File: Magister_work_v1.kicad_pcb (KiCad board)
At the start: 4 copper layers, 50.5 x 81 mm, 151 parts, among them J1 Conn_01x02_Pin, J10 Conn_01x06_Pin, J11 Conn_01x03_Pin, J12 Conn_01x03_Pin, J13 Conn_01x03_Pin, J14 Conn_01x03_Pin, J15 Conn_01x02_Pin, J17 Conn_01x04_Pin, J2 Conn_01x03_Pin, J3 Conn_01x03_Pin, J4 Conn_01x03_Pin, J5 Conn_01x03_Pin, J6 Conn_01x04_Pin, J7 Conn_01x02_Pin, J8 Conn_01x06_Pin, J9 Conn_01x02_Pin, Q1 AO3400A, Q2 AO3400A, U10 LSM6DS3, U11 MPU-6500, U12 BMI270, U2 XC6206P332MR, U3 Ai-Thinker-Ra-01, U4 MCP6001-OT, U5 AMS1117-3.3, U6 XL1509-5.0, U7 STM32F407VETx, U8 AT24C256, U9 Ai-Thinker-Ra-01SH, Y1 X322525MQB4SI, Y2 SMD03215C2

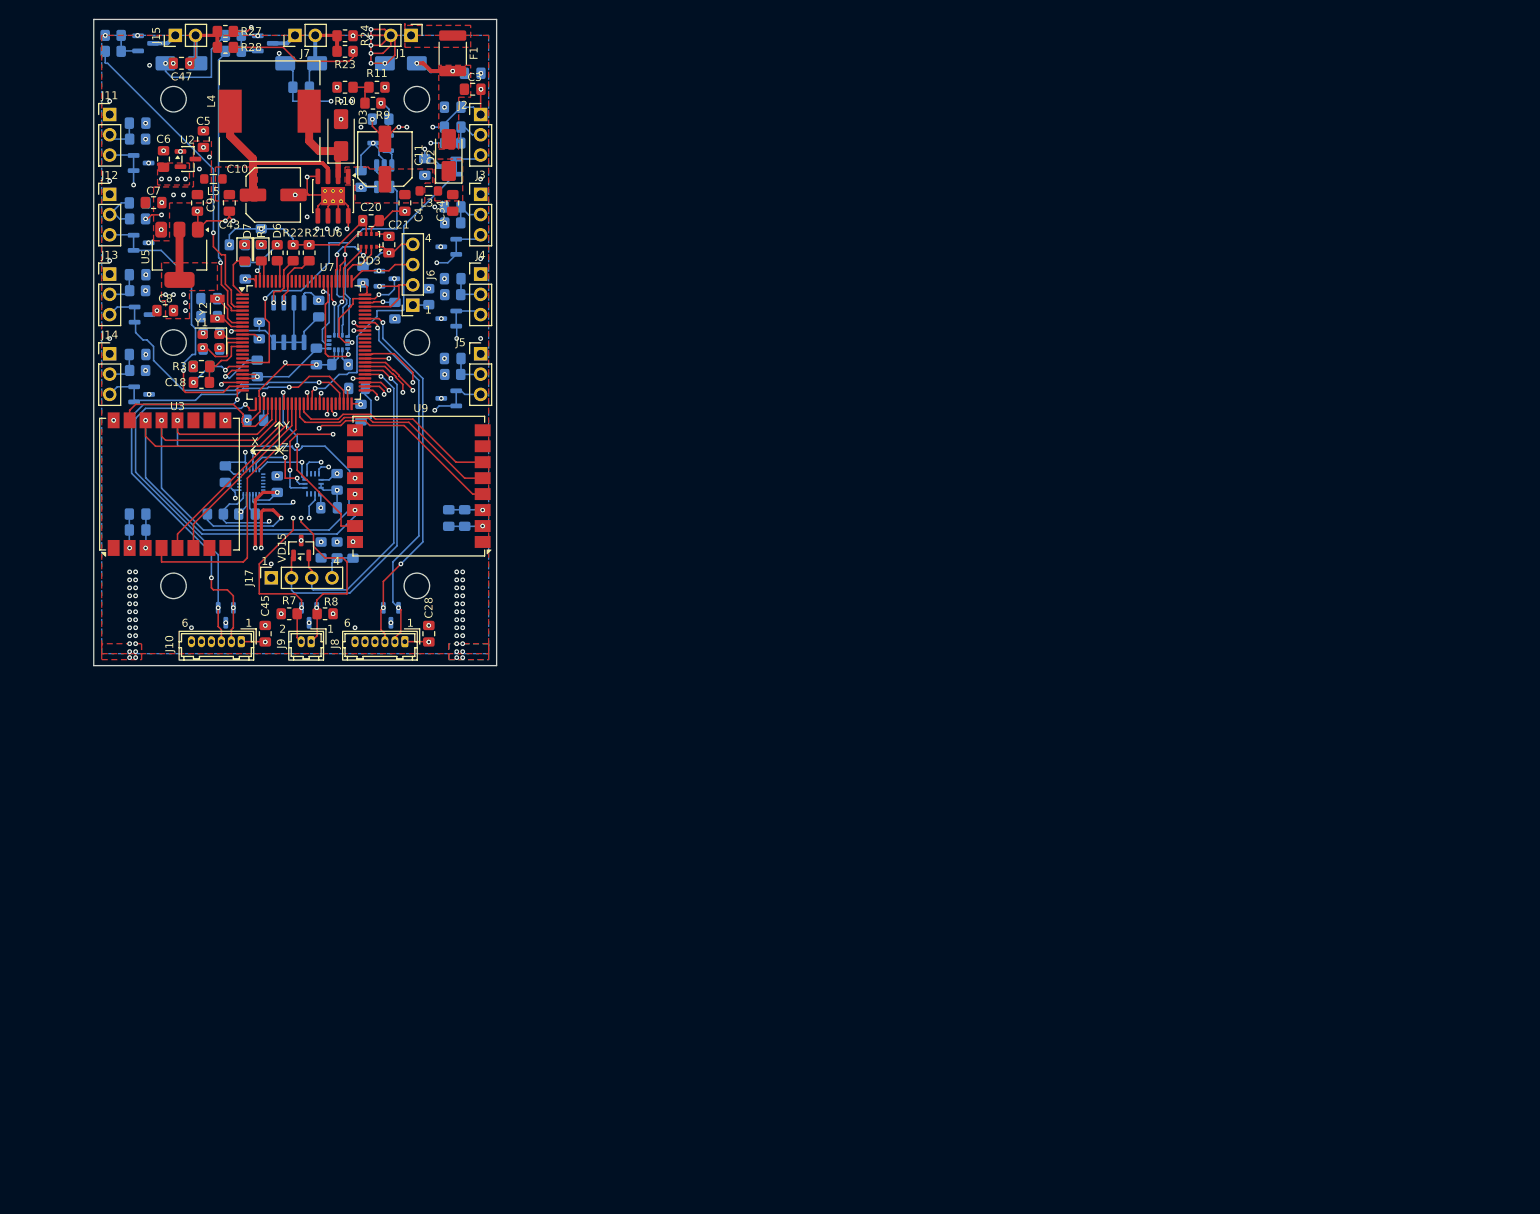
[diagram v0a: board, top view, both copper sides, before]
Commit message: feat:убрал часть с батарейным питанием, убрал лишние элементы со старого проекта
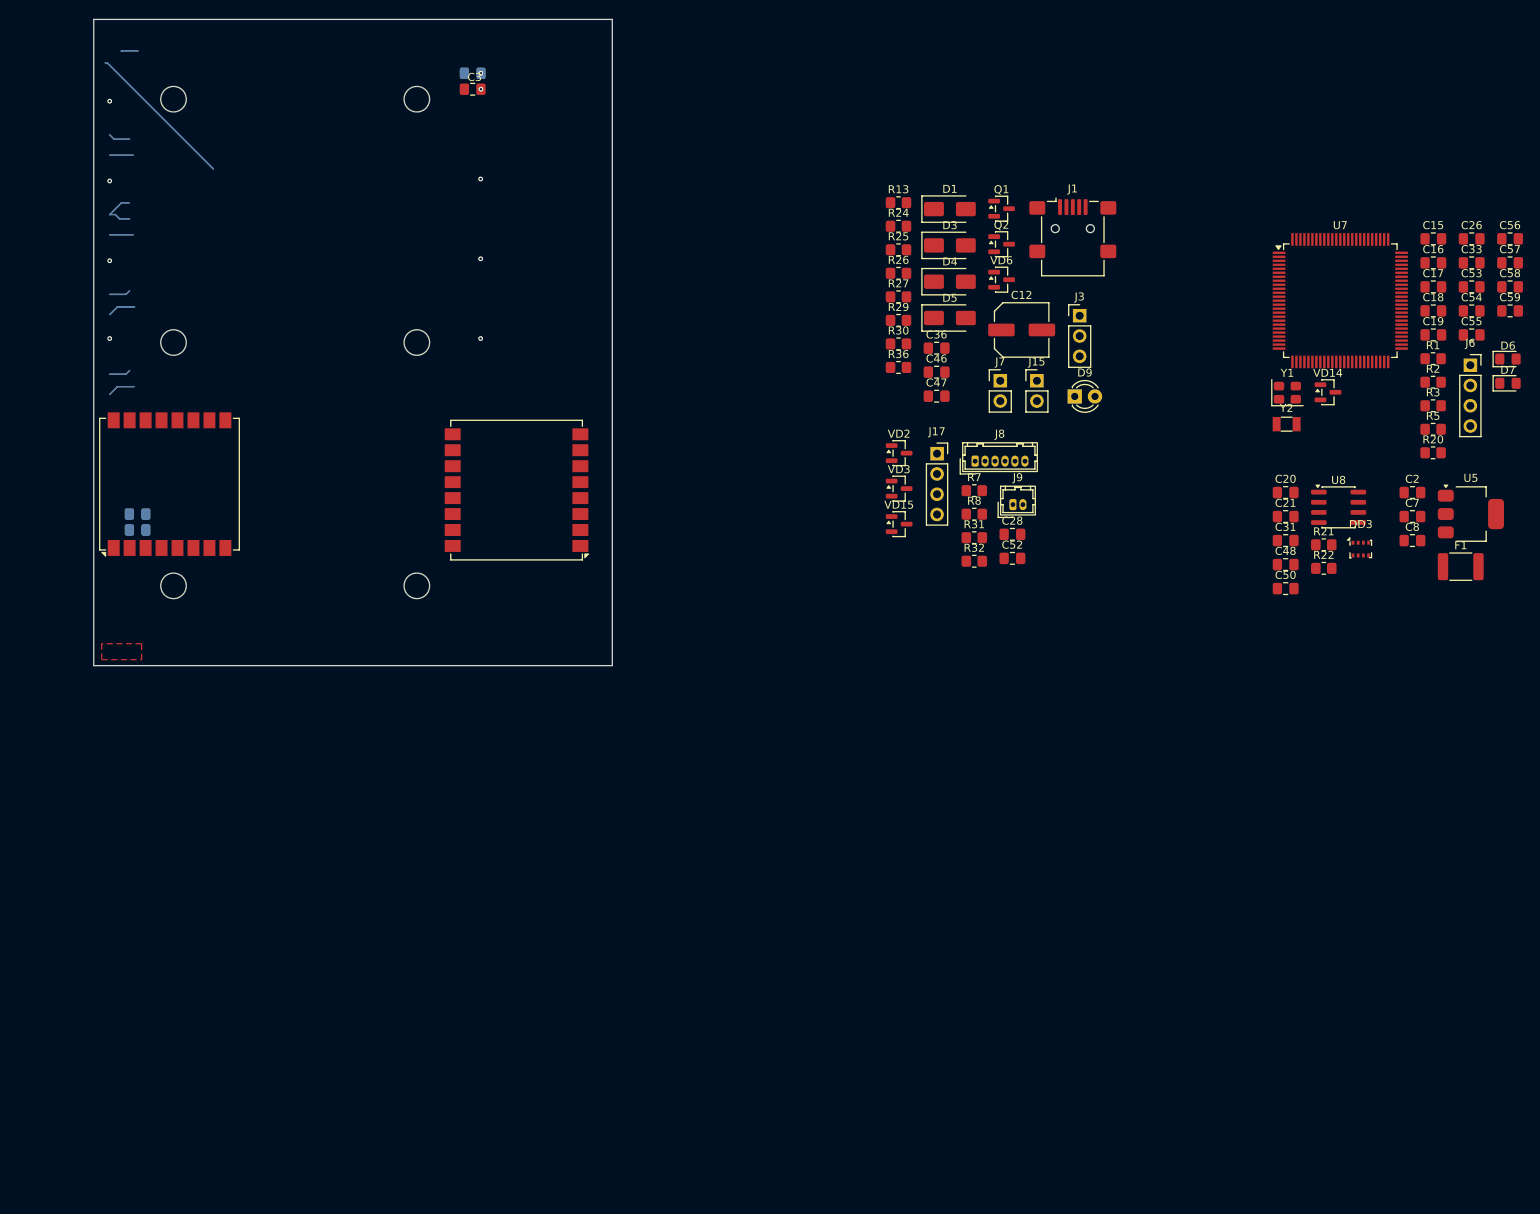
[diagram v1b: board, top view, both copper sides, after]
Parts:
- removed C10, C11: 100u, Capacitor_SMD:C_Elec_6.3x7.7
- removed C14, C22, C23, C24, C25, C27, C29, C30, C34, C35, C37, C38, C39, C4, C40, C41, C42, C43, C44, C45, C5, C51, C6, C9: 0.1u, Capacitor_SMD:C_0805_2012Metric_Pad1.18x1.45mm_HandSolder
- removed D2: SS36, Diode_SMD:D_SMA
- removed J10: Conn_01x06_Pin, Connector_Hirose:Hirose_DF13-06P-1.25DSA_1x06_P1.25mm_Vertical
- removed J11, J12, J13, J14, J2, J4, J5: Conn_01x03_Pin, Connector_PinHeader_2.54mm:PinHeader_1x03_P2.54mm_Vertical
- removed L3, L5: BLM21PG121SN1D, Inductor_SMD:L_0805_2012Metric_Pad1.05x1.20mm_HandSolder
- removed L4: 47uH, Inductor_SMD:L_12x12mm_H8mm
- removed R10: 1k, Resistor_SMD:R_0805_2012Metric_Pad1.20x1.40mm_HandSolder
- removed R11, R4: 10k, Resistor_SMD:R_0805_2012Metric_Pad1.20x1.40mm_HandSolder
- removed R12, R14, R15, R16, R17, R18, R19, R23, R28: 0, Resistor_SMD:R_0805_2012Metric_Pad1.20x1.40mm_HandSolder
- removed R9: 3k, Resistor_SMD:R_0805_2012Metric_Pad1.20x1.40mm_HandSolder
- removed U10: LSM6DS3, Package_LGA:LGA-14_3x2.5mm_P0.5mm_LayoutBorder3x4y
- removed U11: MPU-6500, Sensor_Motion:InvenSense_QFN-24_3x3mm_P0.4mm
- removed U12: BMI270, Package_LGA:Bosch_LGA-14_3x2.5mm_P0.5mm
- removed U2: XC6206P332MR, Package_TO_SOT_SMD:SOT-23
- removed U4: MCP6001-OT, Package_TO_SOT_SMD:SOT-23-5_HandSoldering
- removed U6: XL1509-5.0, Package_SO:SOIC-8-1EP_3.9x4.9mm_P1.27mm_EP2.29x3mm_ThermalVias
- removed VD10, VD11, VD12, VD13, VD4, VD5, VD7, VD8, VD9: GSOT03C-E3-08, Package_TO_SOT_SMD:SOT-23
- added C12: 100u, Capacitor_SMD:C_Elec_6.3x7.7, F.Cu at (146.3, 68.9)
- added D9: LED, LED_THT:LED_D3.0mm_Clear, F.Cu at (153.0, 77.3)
- added R36: 330, Resistor_SMD:R_0805_2012Metric_Pad1.20x1.40mm_HandSolder, F.Cu at (130.9, 73.6)
- C1: value 0.01u -> 0.1u
- C15, C16, C17, C19, C2, C26, C31, C33, C36, C46, C48, C50, C52, C53, C54, C55, C56, C57, C58, C59, D4, D5, Q1, Q2, R13, R2, R20, R25, R26, R29, R30, R31, R32, R5, U8, VD14, VD2, VD3, VD6: moved to F.Cu
- C3: value 1u -> 0.1u
- D1: value SMAJ30CA -> SS32; moved to F.Cu
- D3: value SS36 -> SMAJ5.0CA
- J1: value Conn_01x02_Pin -> USB_B_Mini; footprint Connector_PinHeader_2.54mm:PinHeader_1x02_P2.54mm_Vertical -> Connector_USB:USB_Mini-B_Lumberg_2486_01_Horizontal
- moved U5 165.1 mm to (202.6, 92.0), turned to 0 degrees
- moved C56 163.4 mm to (207.5, 57.5)
- moved C58 163.1 mm to (207.5, 63.5)
- moved C59 163.1 mm to (207.5, 66.5), turned to 0 degrees
- moved C7 162.6 mm to (195.3, 92.3), turned to 0 degrees
- moved C26 160.0 mm to (202.7, 57.5), turned to 0 degrees
- moved D7 159.2 mm to (207.3, 75.6), turned to 0 degrees
- moved C8 159.0 mm to (195.3, 95.3), turned to 0 degrees
- moved C55 158.0 mm to (202.7, 69.5)
- moved D6 156.8 mm to (207.3, 72.6), turned to 0 degrees
- moved C18 154.6 mm to (197.9, 66.5), turned to 0 degrees
- moved R3 154.4 mm to (197.9, 78.4)
- moved C53 153.7 mm to (202.7, 63.5), turned to 0 degrees
- moved C54 152.4 mm to (202.7, 66.5), turned to 0 degrees
- moved C33 152.2 mm to (202.7, 60.5), turned to 0 degrees
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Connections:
- net +12V_1 renamed Net-(F1-A1)
- C1 pad 1: +12V_in -> +5V_in
- C2 pad 1: +12V_in -> +5V_in
- C3 pad 1: +12V_in -> +5V_in
- C8 pad 1: +3V3D -> +3V3
- D1 pad 1: GND -> +5V
- D1 pad 2: +12V_in -> +5V_in
- D3 pad 1: Net-(D3-K) -> GND
- D3 pad 2: GND -> +5V_in
- F1 pad 2: +12V_in -> +5V_in
- J1 pad 2: GND -> unconnected-(J1-D--Pad2)
- U5 pad 2: +3V3D -> +3V3
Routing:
- net GND: track 243.9 -> 0.00 mm, vias 144 -> 9
- net +3V3A: track 154.5 -> 0.00 mm, vias 9 -> 0
- net +5V: track 153.2 -> 0.00 mm, vias 21 -> 0
- net +3V3D: track 124.3 -> 0.00 mm, vias 31 -> 0
- net MOSI_LoRa: track 61.2 -> 0.00 mm, vias 2 -> 0
- net MISO_LoRa: track 57.4 -> 0.00 mm, vias 2 -> 0
- net MPU_INT: track 54.9 -> 0.00 mm, vias 2 -> 0
- net BN_880_SCL: track 54.4 -> 0.00 mm, vias 3 -> 0
- net BN_880_SDA: track 53.3 -> 0.00 mm, vias 3 -> 0
- net DEBUG_TX1: track 50.6 -> 0.00 mm, vias 3 -> 0
- net MPU_CS: track 50.0 -> 0.00 mm, vias 2 -> 0
- net DEBUG_RX1: track 49.5 -> 0.00 mm, vias 2 -> 0
- net BN_880_RX: track 46.9 -> 0.00 mm, vias 3 -> 0
- net BN_880_TX: track 45.6 -> 0.00 mm, vias 2 -> 0
- net PWM1: track 45.3 -> 0.00 mm, vias 1 -> 0
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- removed copper zone on F.Cu, net +12V
- removed copper zone on F.Cu, net +12V_in
- removed copper zone on F.Cu, net +3V3A
- removed copper zone on In2.Cu, net +3V3A
- removed copper zone on F.Cu, net +3V3D
- removed copper zone on In1.Cu, net +3V3D
- removed copper zone on In2.Cu, net +3V3D
- removed copper zone on F.Cu, net +5V
- removed copper zone on In2.Cu, net +5V
- removed copper zone on B.Cu, net GND
- removed copper zone on In2.Cu, net GND
- removed copper zone on F.Cu, net Net-(D2-K)
- removed copper zone on F.Cu, net Net-(F1-A1)
- removed copper zone on F.Cu, net Net-(U6-FB)
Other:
- board size 50.5 x 81 mm -> 65 x 81 mm
- board text removed: "1"
- board text removed: "2"
- board text removed: "4"
- board text removed: "6"
- board text removed: "X"
- board text removed: "Y"
- board text removed: "Z"

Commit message: feaat: добавлены светодиоды, кнопки и недостающие элементы защиты питания
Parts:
- removed R25, R29: 100, Resistor_SMD:R_0805_2012Metric_Pad1.20x1.40mm_HandSolder
- added C4: 0.1u, Capacitor_SMD:C_0805_2012Metric_Pad1.18x1.45mm_HandSolder, F.Cu at (182.7, 155.8)
- added C60: 0.1u, Capacitor_SMD:C_0805_2012Metric_Pad1.18x1.45mm_HandSolder, F.Cu at (130.1, 132.9)
- added C61: 0.1u, Capacitor_SMD:C_0805_2012Metric_Pad1.18x1.45mm_HandSolder, F.Cu at (130.1, 135.9)
- added C62: 0.1u, Capacitor_SMD:C_0805_2012Metric_Pad1.18x1.45mm_HandSolder, F.Cu at (130.1, 138.9)
- added C63: 0.1u, Capacitor_SMD:C_0805_2012Metric_Pad1.18x1.45mm_HandSolder, F.Cu at (130.1, 141.9)
- added C64: 0.1u, Capacitor_SMD:C_0805_2012Metric_Pad1.18x1.45mm_HandSolder, F.Cu at (134.9, 132.9)
- added C65: 0.1u, Capacitor_SMD:C_0805_2012Metric_Pad1.18x1.45mm_HandSolder, F.Cu at (134.9, 135.9)
- added C66: 0.1u, Capacitor_SMD:C_0805_2012Metric_Pad1.18x1.45mm_HandSolder, F.Cu at (134.9, 138.9)
- added C67: 0.1u, Capacitor_SMD:C_0805_2012Metric_Pad1.18x1.45mm_HandSolder, F.Cu at (134.9, 141.9)
- added C68: 0.1u, Capacitor_SMD:C_0805_2012Metric_Pad1.18x1.45mm_HandSolder, F.Cu at (139.7, 132.9)
- added C69: 0.1u, Capacitor_SMD:C_0805_2012Metric_Pad1.18x1.45mm_HandSolder, F.Cu at (139.7, 135.9)
- added C70: 0.1u, Capacitor_SMD:C_0805_2012Metric_Pad1.18x1.45mm_HandSolder, F.Cu at (139.7, 138.9)
- added C71: 0.1u, Capacitor_SMD:C_0805_2012Metric_Pad1.18x1.45mm_HandSolder, F.Cu at (139.7, 141.9)
- added D10: LED, LED_THT:LED_D3.0mm, F.Cu at (173.6, 114.0)
- added D11: LED, LED_THT:LED_D3.0mm, F.Cu at (173.6, 119.4)
- added D12: LED, LED_THT:LED_D3.0mm, F.Cu at (173.6, 124.9)
- added D13: LED, LED_THT:LED_D3.0mm, F.Cu at (173.6, 130.4)
- added D14: LED, LED_THT:LED_D3.0mm, F.Cu at (173.6, 135.8)
- added D15: SMBJ5.0CA, Diode_SMD:D_SMB, F.Cu at (176.1, 152.4)
- added D8: LED, LED_THT:LED_D3.0mm, F.Cu at (173.6, 108.5)
- added Q3: PDTC143ET, Package_TO_SOT_SMD:SOT-23-3, F.Cu at (180.4, 108.0)
- added Q4: PDTC143ET, Package_TO_SOT_SMD:SOT-23-3, F.Cu at (180.4, 112.4)
- added Q5: PDTC143ET, Package_TO_SOT_SMD:SOT-23-3, F.Cu at (180.4, 116.9)
- added Q6: PDTC143ET, Package_TO_SOT_SMD:SOT-23-3, F.Cu at (180.4, 121.3)
- added Q7: PDTC143ET, Package_TO_SOT_SMD:SOT-23-3, F.Cu at (180.4, 125.8)
- added Q8: PDTC143ET, Package_TO_SOT_SMD:SOT-23-3, F.Cu at (180.4, 130.2)
- added R11: 220, Resistor_SMD:R_0805_2012Metric_Pad1.20x1.40mm_HandSolder, F.Cu at (185.3, 113.1)
- added R12: 220, Resistor_SMD:R_0805_2012Metric_Pad1.20x1.40mm_HandSolder, F.Cu at (185.3, 116.1)
- added R14: 220, Resistor_SMD:R_0805_2012Metric_Pad1.20x1.40mm_HandSolder, F.Cu at (185.3, 119.0)
- added R15: 10k, Resistor_SMD:R_0805_2012Metric_Pad1.20x1.40mm_HandSolder, F.Cu at (182.4, 142.0)
- added R16: 220, Resistor_SMD:R_0805_2012Metric_Pad1.20x1.40mm_HandSolder, F.Cu at (185.3, 122.0)
- added R28: 100, Resistor_SMD:R_0805_2012Metric_Pad1.20x1.40mm_HandSolder, F.Cu at (144.5, 132.9)
- added R33: 100, Resistor_SMD:R_0805_2012Metric_Pad1.20x1.40mm_HandSolder, F.Cu at (144.5, 135.8)
- added R34: 100, Resistor_SMD:R_0805_2012Metric_Pad1.20x1.40mm_HandSolder, F.Cu at (144.5, 138.8)
- added R35: 100, Resistor_SMD:R_0805_2012Metric_Pad1.20x1.40mm_HandSolder, F.Cu at (144.5, 141.7)
- added R37: 100, Resistor_SMD:R_0805_2012Metric_Pad1.20x1.40mm_HandSolder, F.Cu at (149.3, 132.9)
- added R38: 100, Resistor_SMD:R_0805_2012Metric_Pad1.20x1.40mm_HandSolder, F.Cu at (149.3, 135.8)
- added R39: 100, Resistor_SMD:R_0805_2012Metric_Pad1.20x1.40mm_HandSolder, F.Cu at (149.3, 138.8)
- added R40: 100, Resistor_SMD:R_0805_2012Metric_Pad1.20x1.40mm_HandSolder, F.Cu at (149.3, 141.7)
- added R41: 100, Resistor_SMD:R_0805_2012Metric_Pad1.20x1.40mm_HandSolder, F.Cu at (154.0, 132.9)
- added R42: 100, Resistor_SMD:R_0805_2012Metric_Pad1.20x1.40mm_HandSolder, F.Cu at (154.0, 135.8)
- added R43: 100, Resistor_SMD:R_0805_2012Metric_Pad1.20x1.40mm_HandSolder, F.Cu at (154.0, 138.8)
- added R44: 100, Resistor_SMD:R_0805_2012Metric_Pad1.20x1.40mm_HandSolder, F.Cu at (154.0, 141.7)
- added R45: 220, Resistor_SMD:R_0805_2012Metric_Pad1.20x1.40mm_HandSolder, F.Cu at (182.4, 145.0)
- added R46: 220, Resistor_SMD:R_0805_2012Metric_Pad1.20x1.40mm_HandSolder, F.Cu at (182.4, 147.9)
- added R6: 220, Resistor_SMD:R_0805_2012Metric_Pad1.20x1.40mm_HandSolder, F.Cu at (185.3, 107.2)
- added R9: 220, Resistor_SMD:R_0805_2012Metric_Pad1.20x1.40mm_HandSolder, F.Cu at (185.3, 110.2)
- added SW1: SW_Push, Button_Switch_THT:SW_PUSH_6mm, F.Cu at (46.2, 50.8)
- added SW10: SW_Push, Button_Switch_THT:SW_PUSH_6mm, F.Cu at (161.4, 107.8)
- added SW11: SW_Push, Button_Switch_THT:SW_PUSH_6mm, F.Cu at (161.4, 116.3)
- added SW12: SW_Push, Button_Switch_THT:SW_PUSH_6mm, F.Cu at (161.4, 124.9)
- added SW2: SW_Push, Button_Switch_THT:SW_PUSH_6mm, F.Cu at (62.2, 50.8)
- added SW3: SW_Push, Button_Switch_THT:SW_PUSH_6mm, F.Cu at (129.7, 124.9)
- added SW4: SW_Push, Button_Switch_THT:SW_PUSH_6mm, F.Cu at (54.2, 43.2)
- added SW5: SW_Push, Button_Switch_THT:SW_PUSH_6mm, F.Cu at (54.2, 58.2)
- added SW6: SW_Push, Button_Switch_THT:SW_PUSH_6mm, F.Cu at (140.3, 124.9)
- added SW7: SW_Push, Button_Switch_THT:SW_PUSH_6mm, F.Cu at (150.8, 107.8)
- added SW8: SW_Push, Button_Switch_THT:SW_PUSH_6mm, F.Cu at (150.8, 116.3)
- added SW9: SW_Push, Button_Switch_THT:SW_PUSH_6mm, F.Cu at (150.8, 124.9)
- added U10: SRV05-4, Package_TO_SOT_SMD:SOT-23-6, F.Cu at (182.9, 152.1)
- added VD10: GSOT03C-E3-08, Package_TO_SOT_SMD:SOT-23_Handsoldering, F.Cu at (124.5, 132.1)
- added VD4: GSOT03C-E3-08, Package_TO_SOT_SMD:SOT-23_Handsoldering, F.Cu at (124.5, 108.2)
- added VD5: GSOT03C-E3-08, Package_TO_SOT_SMD:SOT-23_Handsoldering, F.Cu at (124.5, 113.0)
- added VD7: GSOT03C-E3-08, Package_TO_SOT_SMD:SOT-23_Handsoldering, F.Cu at (124.5, 117.8)
- added VD8: GSOT03C-E3-08, Package_TO_SOT_SMD:SOT-23_Handsoldering, F.Cu at (124.5, 122.6)
- added VD9: GSOT03C-E3-08, Package_TO_SOT_SMD:SOT-23_Handsoldering, F.Cu at (124.5, 127.3)
- D4, D5: value SMAJ30CA -> SMAJ5.0CA
- R36: value 330 -> 220
- moved D5 88.8 mm to (176.0, 147.4)
- moved D4 88.8 mm to (176.0, 142.8)
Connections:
- J1 pad SH: Earth -> PE
- R31 pad 1: +3V3D -> +3V3
